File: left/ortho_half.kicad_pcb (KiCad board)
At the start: 2 copper layers, 150.9 x 145.7 mm, 77 parts, among them J1 AudioJack4, J10 Conn_01x04, J11 Conn_01x01, J12 Conn_01x02, J13 Conn_01x01, J14 Conn_01x01, J15 Conn_01x01, J16 Conn_01x01, J17 Conn_01x01, J18 Conn_01x01, J19 Conn_01x01, J2 Conn_01x01, J20 Conn_01x01, J21 Conn_01x01, J3 Conn_01x01, J4 Conn_01x01, J5 Conn_01x01, J6 Conn_01x01, J7 Conn_01x01, J8 Conn_01x01, J9 Conn_01x01, K11 KEYSW_RGB, K12 KEYSW_RGB, K13 KEYSW_RGB, K14 KEYSW_RGB, K15 KEYSW_RGB, K16 KEYSW_RGB, K21 KEYSW_RGB, K22 KEYSW_RGB, K23 KEYSW_RGB, K24 KEYSW_RGB, K25 KEYSW_RGB, K26 KEYSW_RGB, K31 KEYSW_RGB, K32 KEYSW_RGB, K33 KEYSW_RGB, K34 KEYSW_RGB, K35 KEYSW_RGB, K36 KEYSW_RGB, K41 KEYSW_RGB, K42 KEYSW_RGB, K43 KEYSW_RGB, K44 KEYSW_RGB, K45 KEYSW_RGB, K46 KEYSW_RGB, K51 KEYSW_RGB, K52 KEYSW_RGB, K53 KEYSW_RGB, K54 KEYSW_RGB, K55 KEYSW_RGB, K56 KEYSW_RGB, K61 KEYSW_RGB, K62 KEYSW_RGB, K63 KEYSW_RGB, K64 KEYSW_RGB, K65 KEYSW_RGB, K66 KEYSW_RGB, SW1 SW_PUSH_RESET, SW2 Rotary_Encoder_Switch, SW4 SW_SPST, SW5 SW_SPST, SW6 SW_SPST, U1 microctrl_superset, U2 IS31FL3733-TQ

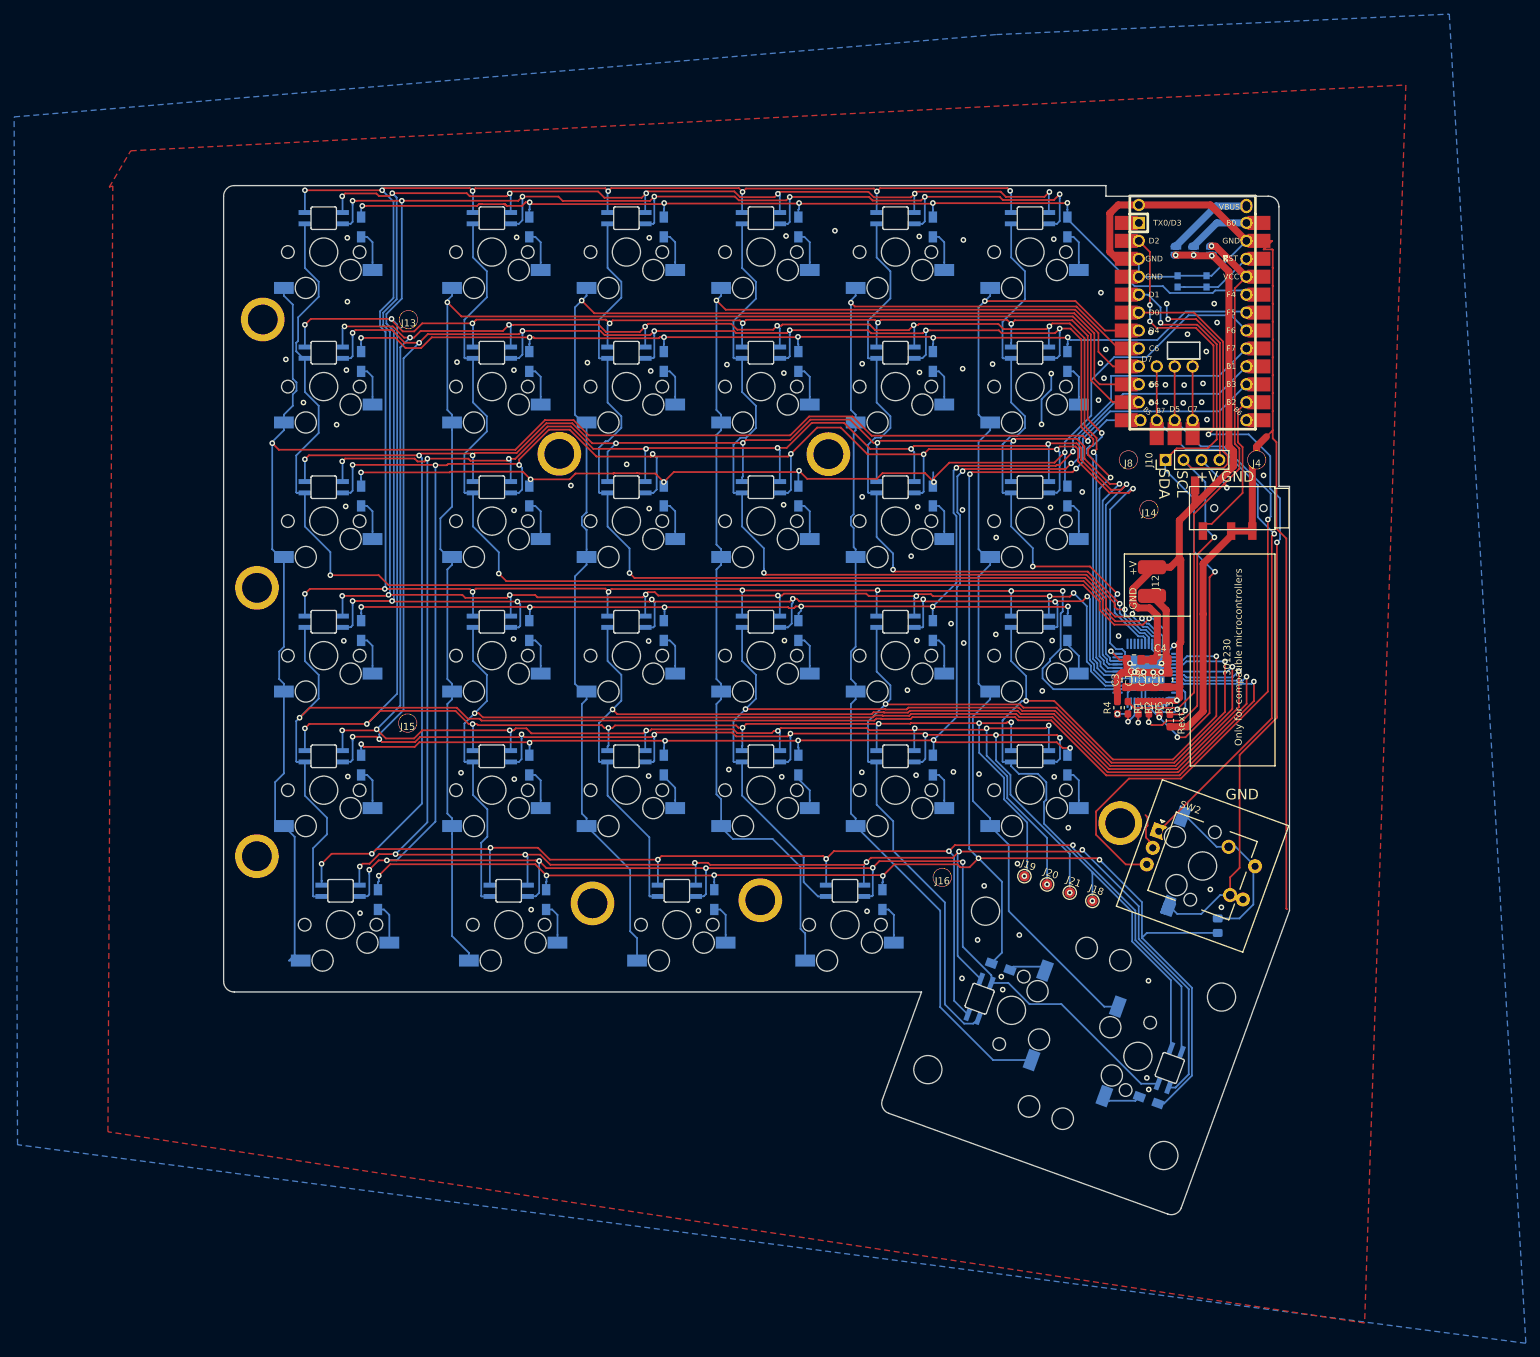
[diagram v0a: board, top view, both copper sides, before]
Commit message: Broke out keys into individual components so that the BOM and pick and place are easier to generate.
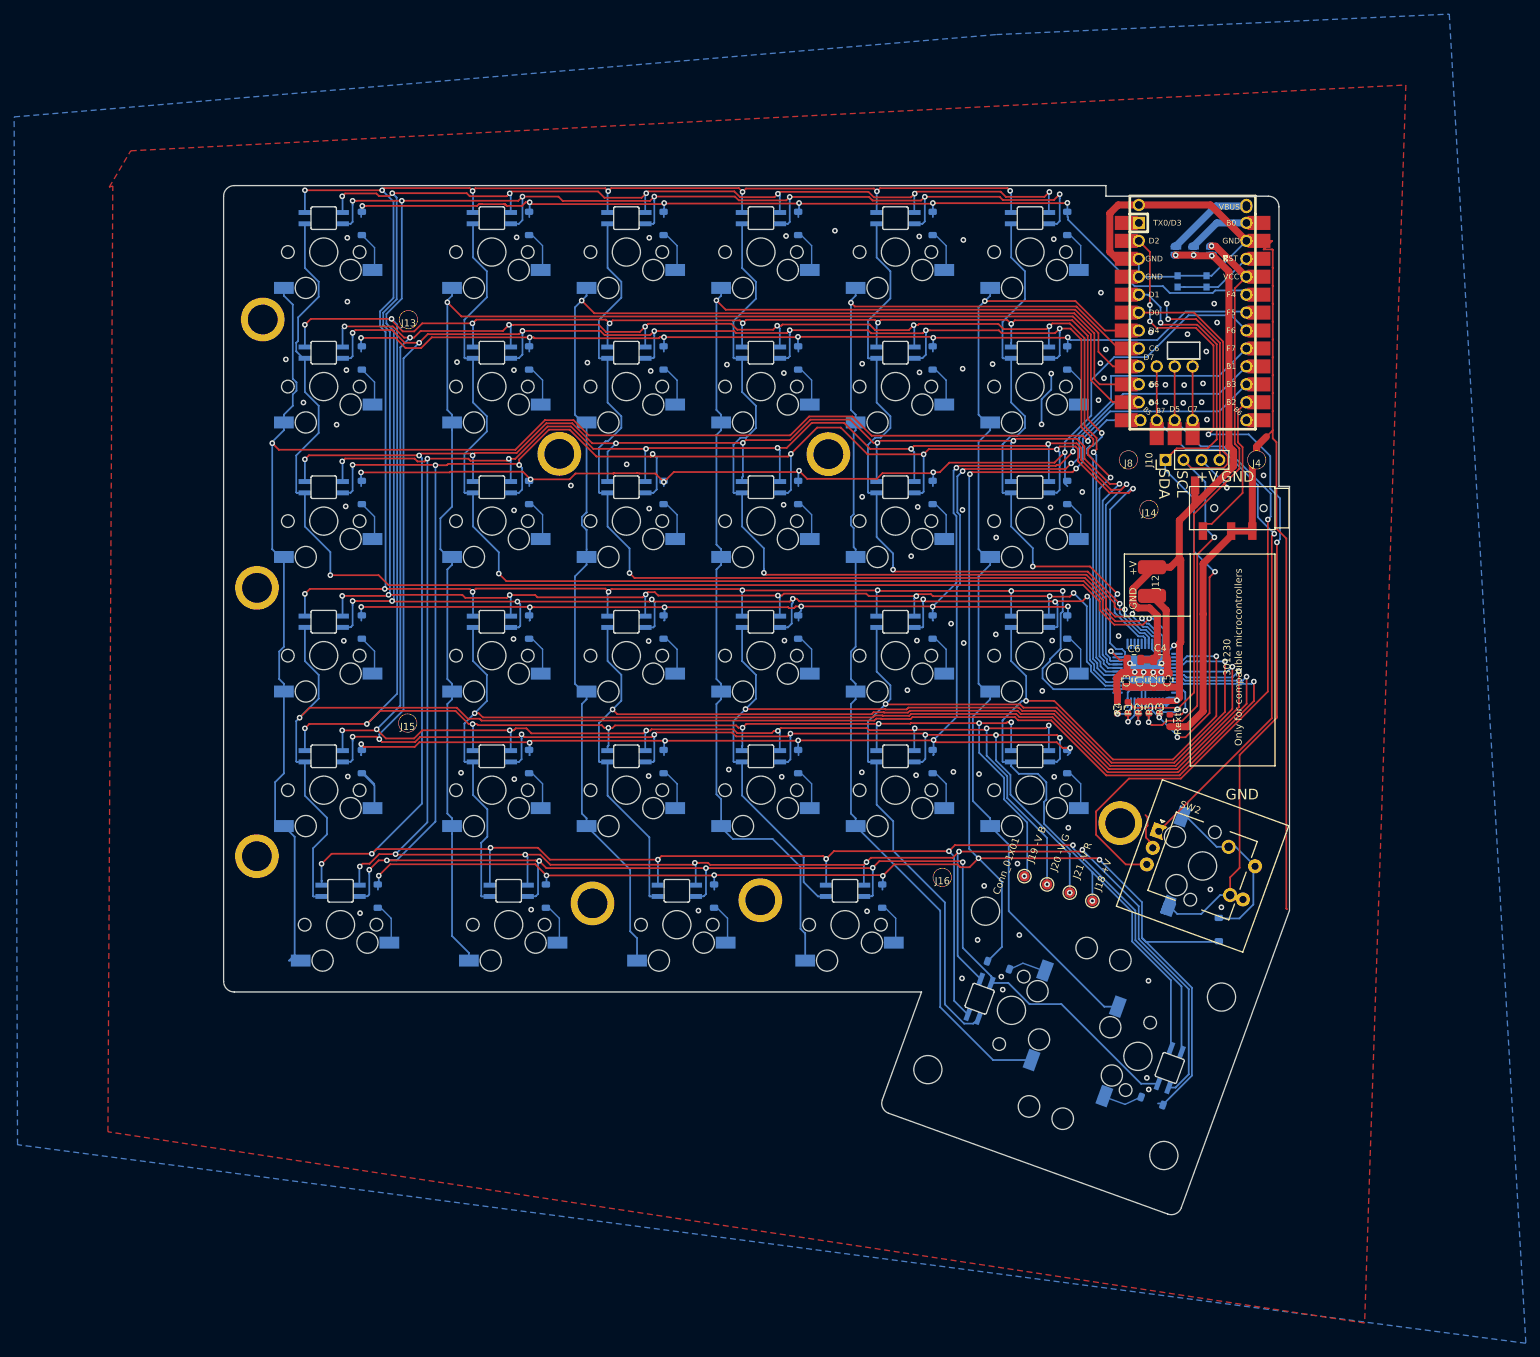
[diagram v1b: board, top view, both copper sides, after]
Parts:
- removed D1: DIODE, Diode_SMD:D_0805_2012Metric_Pad1.15x1.40mm_HandSolder
- added D11: LED_ARGB, vladkvit_keyb:MX_RGB, F.Cu at (19.1, 23.8)
- added D111: D, Diode_SMD:D_SOD-123, B.Cu at (24.4, 19.8)
- added D12: LED_ARGB, vladkvit_keyb:MX_RGB, F.Cu at (42.9, 23.8)
- added D121: D, Diode_SMD:D_SOD-123, B.Cu at (48.1, 19.8)
- added D13: LED_ARGB, vladkvit_keyb:MX_RGB, F.Cu at (61.9, 23.8)
- added D131: D, Diode_SMD:D_SOD-123, B.Cu at (67.2, 19.8)
- added D14: LED_ARGB, vladkvit_keyb:MX_RGB, F.Cu at (81.0, 23.8)
- added D141: D, Diode_SMD:D_SOD-123, B.Cu at (86.2, 19.8)
- added D15: LED_ARGB, vladkvit_keyb:MX_RGB, F.Cu at (100.0, 23.8)
- added D151: D, Diode_SMD:D_SOD-123, B.Cu at (105.3, 19.8)
- added D16: LED_ARGB, vladkvit_keyb:MX_RGB, F.Cu at (119.1, 23.8)
- added D161: D, Diode_SMD:D_SOD-123, B.Cu at (124.3, 19.8)
- added D21: LED_ARGB, vladkvit_keyb:MX_RGB, F.Cu at (19.1, 42.9)
- added D211: D, Diode_SMD:D_SOD-123, B.Cu at (24.4, 38.8)
- added D22: LED_ARGB, vladkvit_keyb:MX_RGB, F.Cu at (42.9, 42.9)
- added D221: D, Diode_SMD:D_SOD-123, B.Cu at (48.1, 38.8)
- added D23: LED_ARGB, vladkvit_keyb:MX_RGB, F.Cu at (61.9, 42.9)
- added D231: D, Diode_SMD:D_SOD-123, B.Cu at (67.2, 38.8)
- added D24: LED_ARGB, vladkvit_keyb:MX_RGB, F.Cu at (81.0, 42.9)
- added D241: D, Diode_SMD:D_SOD-123, B.Cu at (86.2, 38.8)
- added D25: LED_ARGB, vladkvit_keyb:MX_RGB, F.Cu at (100.0, 42.9)
- added D251: D, Diode_SMD:D_SOD-123, B.Cu at (105.3, 38.8)
- added D26: LED_ARGB, vladkvit_keyb:MX_RGB, F.Cu at (119.1, 42.9)
- added D261: D, Diode_SMD:D_SOD-123, B.Cu at (124.3, 38.8)
- added D31: LED_ARGB, vladkvit_keyb:MX_RGB, F.Cu at (19.1, 61.9)
- added D311: D, Diode_SMD:D_SOD-123, B.Cu at (24.4, 57.9)
- added D32: LED_ARGB, vladkvit_keyb:MX_RGB, F.Cu at (42.9, 61.9)
- added D321: D, Diode_SMD:D_SOD-123, B.Cu at (48.1, 57.9)
- added D33: LED_ARGB, vladkvit_keyb:MX_RGB, F.Cu at (61.9, 61.9)
- added D331: D, Diode_SMD:D_SOD-123, B.Cu at (67.2, 57.9)
- added D34: LED_ARGB, vladkvit_keyb:MX_RGB, F.Cu at (81.0, 61.9)
- added D341: D, Diode_SMD:D_SOD-123, B.Cu at (86.2, 57.9)
- added D35: LED_ARGB, vladkvit_keyb:MX_RGB, F.Cu at (100.0, 61.9)
- added D351: D, Diode_SMD:D_SOD-123, B.Cu at (105.3, 57.9)
- added D36: LED_ARGB, vladkvit_keyb:MX_RGB, F.Cu at (119.1, 61.9)
- added D361: D, Diode_SMD:D_SOD-123, B.Cu at (124.3, 57.9)
- added D41: LED_ARGB, vladkvit_keyb:MX_RGB, F.Cu at (19.1, 81.0)
- added D411: D, Diode_SMD:D_SOD-123, B.Cu at (24.4, 76.9)
- added D42: LED_ARGB, vladkvit_keyb:MX_RGB, F.Cu at (42.9, 81.0)
- added D421: D, Diode_SMD:D_SOD-123, B.Cu at (48.1, 76.9)
- added D43: LED_ARGB, vladkvit_keyb:MX_RGB, F.Cu at (61.9, 81.0)
- added D431: D, Diode_SMD:D_SOD-123, B.Cu at (67.2, 76.9)
- added D44: LED_ARGB, vladkvit_keyb:MX_RGB, F.Cu at (81.0, 81.0)
- added D441: D, Diode_SMD:D_SOD-123, B.Cu at (86.2, 76.9)
- added D45: LED_ARGB, vladkvit_keyb:MX_RGB, F.Cu at (100.0, 81.0)
- added D451: D, Diode_SMD:D_SOD-123, B.Cu at (105.3, 76.9)
- added D46: LED_ARGB, vladkvit_keyb:MX_RGB, F.Cu at (119.1, 81.0)
- added D461: D, Diode_SMD:D_SOD-123, B.Cu at (124.3, 76.9)
- added D51: LED_ARGB, vladkvit_keyb:MX_RGB, F.Cu at (19.1, 100.0)
- added D511: D, Diode_SMD:D_SOD-123, B.Cu at (24.5, 96.0)
- added D52: LED_ARGB, vladkvit_keyb:MX_RGB, F.Cu at (42.9, 100.0)
- added D521: D, Diode_SMD:D_SOD-123, B.Cu at (48.1, 96.0)
- added D53: LED_ARGB, vladkvit_keyb:MX_RGB, F.Cu at (61.9, 100.0)
- added D531: D, Diode_SMD:D_SOD-123, B.Cu at (67.2, 96.0)
- added D54: LED_ARGB, vladkvit_keyb:MX_RGB, F.Cu at (81.0, 100.0)
- added D541: D, Diode_SMD:D_SOD-123, B.Cu at (86.2, 96.0)
- added D55: LED_ARGB, vladkvit_keyb:MX_RGB, F.Cu at (100.0, 100.0)
- added D551: D, Diode_SMD:D_SOD-123, B.Cu at (105.3, 96.0)
- added D56: LED_ARGB, vladkvit_keyb:MX_RGB, F.Cu at (119.1, 100.0)
- added D561: D, Diode_SMD:D_SOD-123, B.Cu at (124.3, 96.0)
- added D571: DIODE, Diode_SMD:D_SOD-123, B.Cu at (145.8, 119.8)
- added D61: LED_ARGB, vladkvit_keyb:MX_RGB, F.Cu at (21.4, 119.1)
- added D611: D, Diode_SMD:D_SOD-123, B.Cu at (26.7, 115.0)
- added D62: LED_ARGB, vladkvit_keyb:MX_RGB, F.Cu at (45.2, 119.1)
- added D621: D, Diode_SMD:D_SOD-123, B.Cu at (50.5, 115.0)
- added D63: LED_ARGB, vladkvit_keyb:MX_RGB, F.Cu at (69.1, 119.1)
- added D631: D, Diode_SMD:D_SOD-123, B.Cu at (74.3, 115.0)
- added D64: LED_ARGB, vladkvit_keyb:MX_RGB, F.Cu at (92.9, 119.1)
- added D641: D, Diode_SMD:D_SOD-123, B.Cu at (98.1, 115.0)
- added D65: LED_ARGB, vladkvit_keyb:MX_RGB, F.Cu at (116.4, 131.2)
- added D651: D, Diode_SMD:D_SOD-123, B.Cu at (114.6, 124.8)
- added D66: LED_ARGB, vladkvit_keyb:MX_RGB, F.Cu at (134.3, 137.7)
- added D661: D, Diode_SMD:D_SOD-123, B.Cu at (136.3, 144.0)
- C1, C2, C3, C4, C5, C6: footprint Capacitor_SMD:C_0805_2012Metric_Pad1.15x1.40mm_HandSolder -> Capacitor_SMD:C_0805_2012Metric
- K11, K21, K31, K41, K51: value KEYSW_RGB -> KEYSW; footprint vladkvit_keyb:Hybrid_PCB_150H_hotswap_diode_RGB_rot -> vladkvit_keyb:MX_switch_hotswap_150
- K12, K13, K14, K15, K16, K22, K23, K24, K25, K26, K32, K33, K34, K35, K36, K42, K43, K44, K45, K46, K52, K53, K54, K55, K56: value KEYSW_RGB -> KEYSW; footprint vladkvit_keyb:Hybrid_PCB_100H_hotswap_diode_RGB_rot -> vladkvit_keyb:MX_switch_hotswap
- K61, K62, K63, K64: value KEYSW_RGB -> KEYSW; footprint vladkvit_keyb:Hybrid_PCB_125H_hotswap_diode_RGB_rot -> vladkvit_keyb:MX_switch_hotswap_125
- K65, K66: value KEYSW_RGB -> KEYSW; footprint vladkvit_keyb:Hybrid_PCB_200H_hotswap_diode_RGB -> vladkvit_keyb:MX_switch_hotswap_200
- R1, R2, R3, R4, R5, Rext1: footprint Resistor_SMD:R_0603_1608Metric_Pad1.05x0.95mm_HandSolder -> Resistor_SMD:R_0603_1608Metric
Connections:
- J10 pad 1: SDA -> SCL
- K11 pad 2: Net-(K11-Pad2) -> Net-(D111-A)
- K12 pad 2: Net-(K12-Pad2) -> Net-(D121-A)
- K13 pad 2: Net-(K13-Pad2) -> Net-(D131-A)
- K14 pad 2: Net-(K14-Pad2) -> Net-(D141-A)
- K15 pad 2: Net-(K15-Pad2) -> Net-(D151-A)
- K16 pad 2: Net-(K16-Pad2) -> Net-(D161-A)
- K21 pad 2: Net-(K21-Pad2) -> Net-(D211-A)
- K22 pad 2: Net-(K22-Pad2) -> Net-(D221-A)
- K23 pad 2: Net-(K23-Pad2) -> Net-(D231-A)
- K24 pad 2: Net-(K24-Pad2) -> Net-(D241-A)
- K25 pad 2: Net-(K25-Pad2) -> Net-(D251-A)
- K26 pad 2: Net-(K26-Pad2) -> Net-(D261-A)
- K31 pad 2: Net-(K31-Pad2) -> Net-(D311-A)
- K32 pad 2: Net-(K32-Pad2) -> Net-(D321-A)
- K33 pad 2: Net-(K33-Pad2) -> Net-(D331-A)
- K34 pad 2: Net-(K34-Pad2) -> Net-(D341-A)
- K35 pad 2: Net-(K35-Pad2) -> Net-(D351-A)
- K36 pad 2: Net-(K36-Pad2) -> Net-(D361-A)
- K41 pad 2: Net-(K41-Pad2) -> Net-(D411-A)
- K42 pad 2: Net-(K42-Pad2) -> Net-(D421-A)
- K43 pad 2: Net-(K43-Pad2) -> Net-(D431-A)
- K44 pad 2: Net-(K44-Pad2) -> Net-(D441-A)
- K45 pad 2: Net-(K45-Pad2) -> Net-(D451-A)
- K46 pad 2: Net-(K46-Pad2) -> Net-(D461-A)
- K51 pad 2: Net-(K51-Pad2) -> Net-(D511-A)
- K52 pad 2: Net-(K52-Pad2) -> Net-(D521-A)
- K53 pad 2: Net-(K53-Pad2) -> Net-(D531-A)
- K54 pad 2: Net-(K54-Pad2) -> Net-(D541-A)
- K55 pad 2: Net-(K55-Pad2) -> Net-(D551-A)
- K56 pad 2: Net-(K56-Pad2) -> Net-(D561-A)
- K61 pad 2: Net-(K61-Pad2) -> Net-(D611-A)
- K62 pad 2: Net-(K62-Pad2) -> Net-(D621-A)
- K63 pad 2: Net-(K63-Pad2) -> Net-(D631-A)
- K64 pad 2: Net-(K64-Pad2) -> Net-(D641-A)
- K65 pad 2: Net-(K65-Pad2) -> Net-(D651-A)
- K66 pad 2: Net-(K66-Pad2) -> Net-(D661-A)
- R3 pad 2: SDA -> SCL
- U1 pad 5: SDA -> SCL
- U2 pad 41: SDA -> SCL
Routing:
- net SDA: track 91.0 -> 0.00 mm, vias 4 -> 0
- net SCL: track 89.8 -> 180.9 mm, vias 2 -> 6
- net Net-(D511-A): track 0.00 -> 10.4 mm
- net Net-(K62-Pad2): track 5.86 -> 0.00 mm
- net Net-(K61-Pad2): track 5.86 -> 0.00 mm
- net Net-(K36-Pad2): track 5.86 -> 0.00 mm
- net Net-(K35-Pad2): track 5.86 -> 0.00 mm
- net Net-(K26-Pad2): track 5.86 -> 0.00 mm
- net Net-(K25-Pad2): track 5.86 -> 0.00 mm
- net Net-(K56-Pad2): track 5.86 -> 0.00 mm
- net Net-(K55-Pad2): track 5.86 -> 0.00 mm
- net Net-(K45-Pad2): track 5.86 -> 0.00 mm
- net Net-(K32-Pad2): track 5.86 -> 0.00 mm
- net Net-(K22-Pad2): track 5.86 -> 0.00 mm
- net Net-(K16-Pad2): track 5.86 -> 0.00 mm
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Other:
- rule pad_to_mask_clearance: 0.051 -> 0
- board text added: "A: nice!nano/ VCC"
- board text added: "B: Pro Micro/ RAW"
- board text added: "C: Elite C/ VBUS"
- board text removed: "Elite C/ VBUS"
- board text removed: "Pro Micro/ RAW"
- board text removed: "nice!nano/ VCC"

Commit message: Kicad 9 upgrade.
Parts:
- C1, C2, C3: value CP -> 0.47 uF
- C4, C5, C6: value CP -> 0.1 uF
- moved C5 0.09 mm to (138.6, 84.4)
- moved C3 0.06 mm to (132.7, 84.4)
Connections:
- D63 pad 2: /Switches/hierarchical_keys32/RGB_R -> led_row3C
- D63 pad 3: /Switches/hierarchical_keys32/RGB_G -> led_row3B
- D63 pad 4: /Switches/hierarchical_keys32/RGB_B -> led_row3A
- D64 pad 2: /Switches/hierarchical_keys33/RGB_R -> led_row3C
- D64 pad 3: /Switches/hierarchical_keys33/RGB_G -> led_row3B
- D64 pad 4: /Switches/hierarchical_keys33/RGB_B -> led_row3A
- D65 pad 2: /Switches/hierarchical_keys34/RGB_R -> led_row3C
- D65 pad 3: /Switches/hierarchical_keys34/RGB_G -> led_row3B
- D65 pad 4: /Switches/hierarchical_keys34/RGB_B -> led_row3A
- D66 pad 2: /Switches/hierarchical_keys35/RGB_R -> led_row3C
- D66 pad 3: /Switches/hierarchical_keys35/RGB_G -> led_row3B
- D66 pad 4: /Switches/hierarchical_keys35/RGB_B -> led_row3A
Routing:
- net row5: track 202.4 -> 196.7 mm
- net row4: track 186.7 -> 182.0 mm
- net row2: track 142.6 -> 138.2 mm
- net row6: track 286.0 -> 282.0 mm
- net row1: track 144.5 -> 140.8 mm
- net row3: track 156.7 -> 153.6 mm
- net unconnected-(U1-B6-Pad13)_1: track 1.78 -> 0.00 mm
- net SCL: track 180.9 -> 182.3 mm
- net col5: track 168.5 -> 169.2 mm
- net led_row2B: track 383.3 -> 382.6 mm
- net led_col4: track 118.6 -> 119.1 mm
- net led_col3: track 138.5 -> 139.0 mm
- net GND: track 299.0 -> 299.3 mm, vias 105 -> 106
- net led_col13: track 135.6 -> 135.3 mm, vias 3 -> 2
- net led_col14: vias 4 -> 3

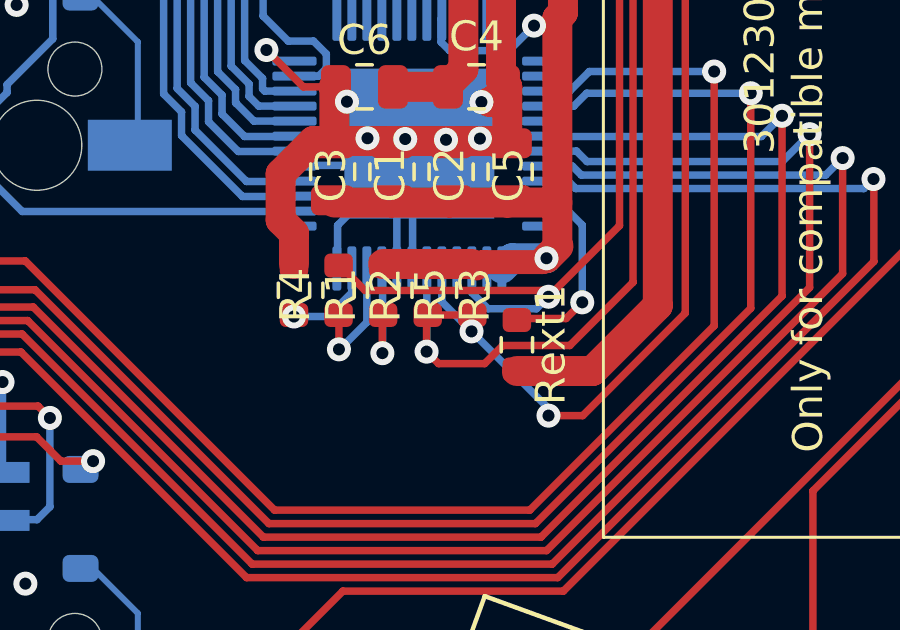
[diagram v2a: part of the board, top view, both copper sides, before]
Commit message: Fix SDA/SCL bug
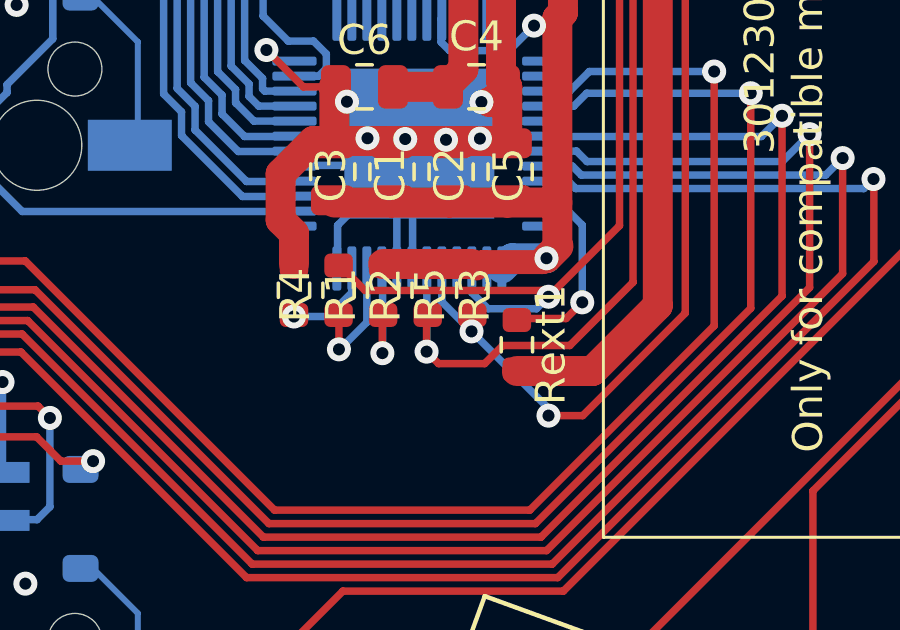
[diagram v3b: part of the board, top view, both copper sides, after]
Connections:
- J10 pad 1: SCL -> SDA
- R3 pad 2: SCL -> SDA
- U1 pad 5: SCL -> SDA
- U2 pad 41: SCL -> SDA
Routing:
- net SCL: track 182.3 -> 89.8 mm, vias 6 -> 2
- net SDA: track 0.00 -> 91.0 mm, vias 0 -> 4

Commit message: checking stuff in
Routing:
- net led_row3C: track 404.9 -> 399.4 mm
- net led_row3B: track 413.5 -> 408.9 mm
- net led_row3A: track 427.7 -> 425.2 mm
- net led_row2C: track 406.9 -> 405.8 mm
- net GND: vias 106 -> 109
